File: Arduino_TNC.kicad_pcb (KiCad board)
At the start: 2 copper layers, 11 parts, among them J1 3.5MM TX, J2 3.5mm RX, Q1 2N2222

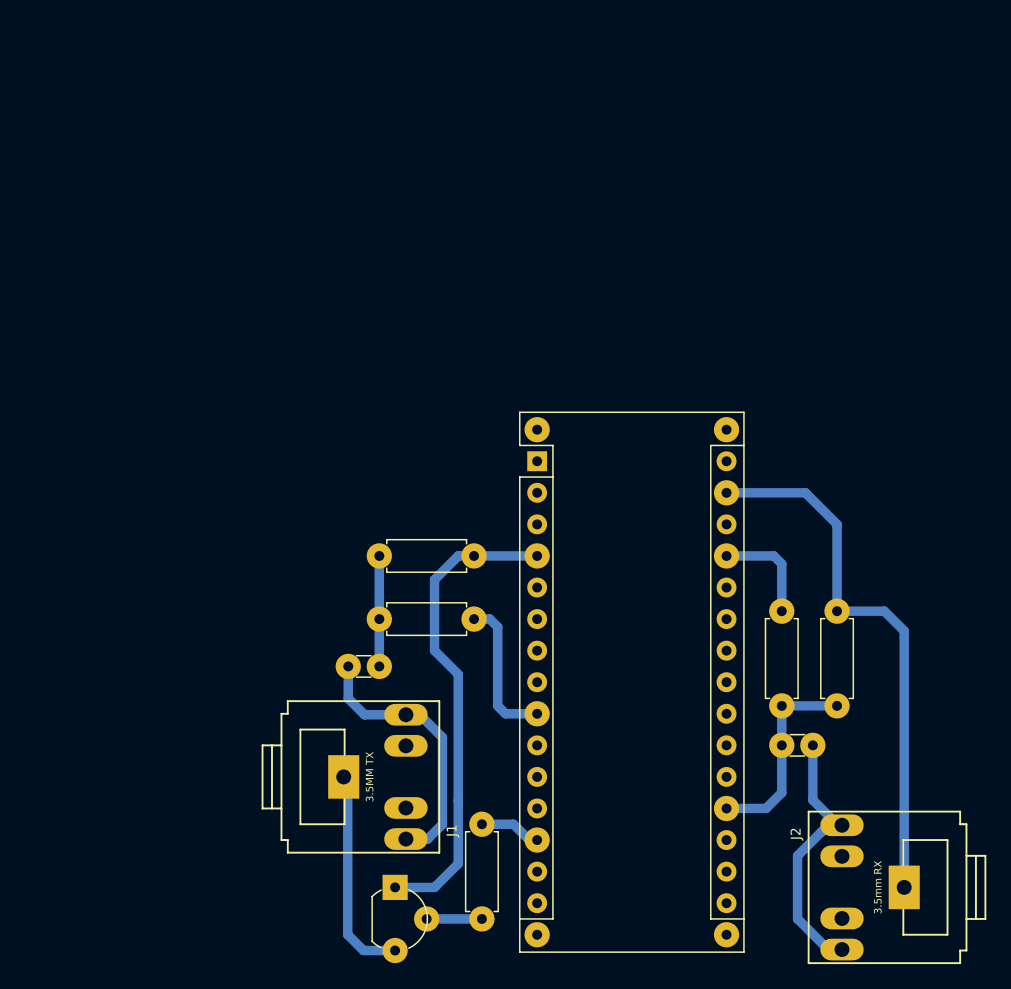
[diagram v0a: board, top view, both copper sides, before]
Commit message: Add proper printable PCB board
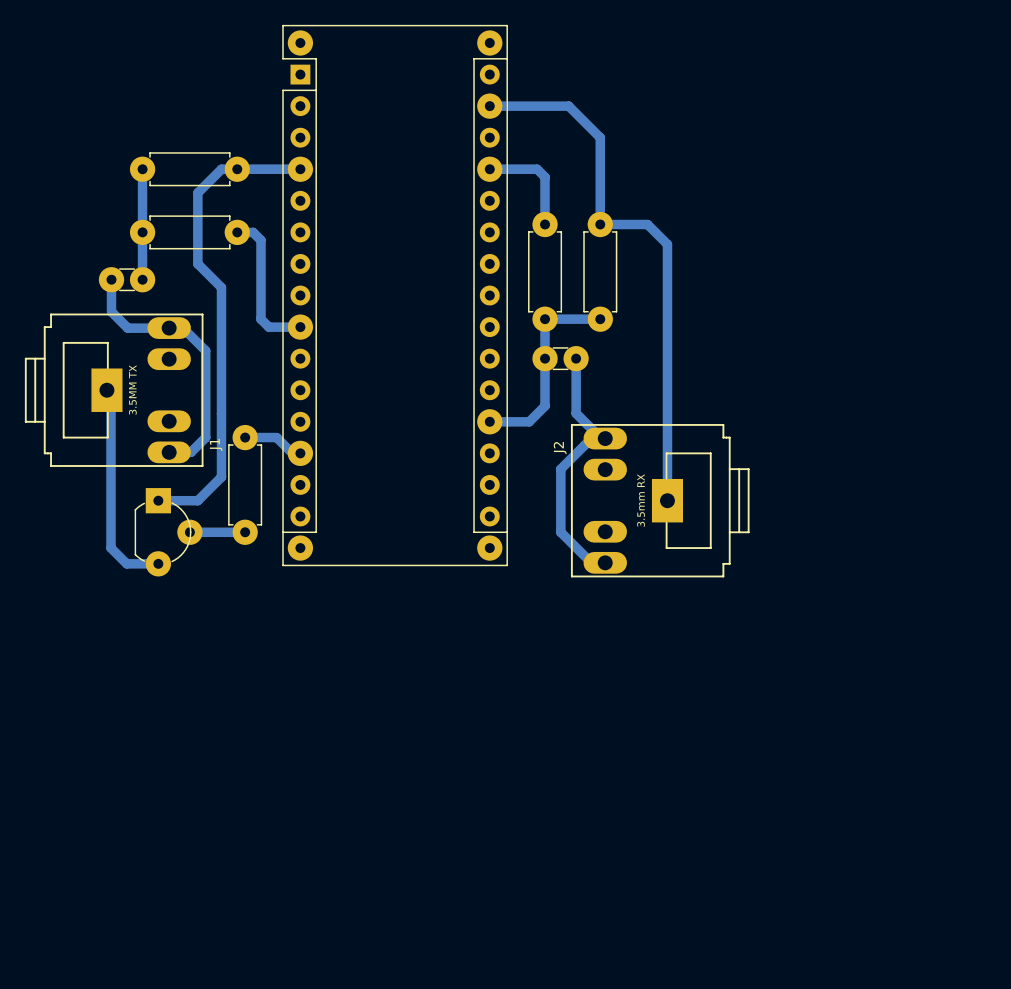
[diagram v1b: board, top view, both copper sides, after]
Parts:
- moved C1 36.5 mm to (117.5, 90.8)
- moved J1 36.5 mm to (116.2, 99.7)
- moved R1 36.5 mm to (125.1, 81.9)
- moved R2 36.5 mm to (125.1, 87.0)
- moved R3 36.5 mm to (125.7, 103.5)
- moved C2 36.5 mm to (149.9, 97.2)
- moved ARDUINO NANO 36.5 mm to (130.2, 74.3)
- moved J2 36.5 mm to (158.1, 108.6)
- moved Q1 36.5 mm to (118.7, 108.6)
- moved R4 36.5 mm to (149.9, 86.4)
- moved R5 36.5 mm to (154.3, 86.4)
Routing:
- net Net-(ARDUINO1-Pad29): track 6.35 -> 9.94 mm
- net GND: track 75.8 -> 72.2 mm
